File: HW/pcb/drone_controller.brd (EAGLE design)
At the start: 46.1 x 88.9 mm, 20 parts, among them J1 SM08B-SRSS-TB, U1 ICM-20600, U2 VXO7805-500, U3 CD40109BE

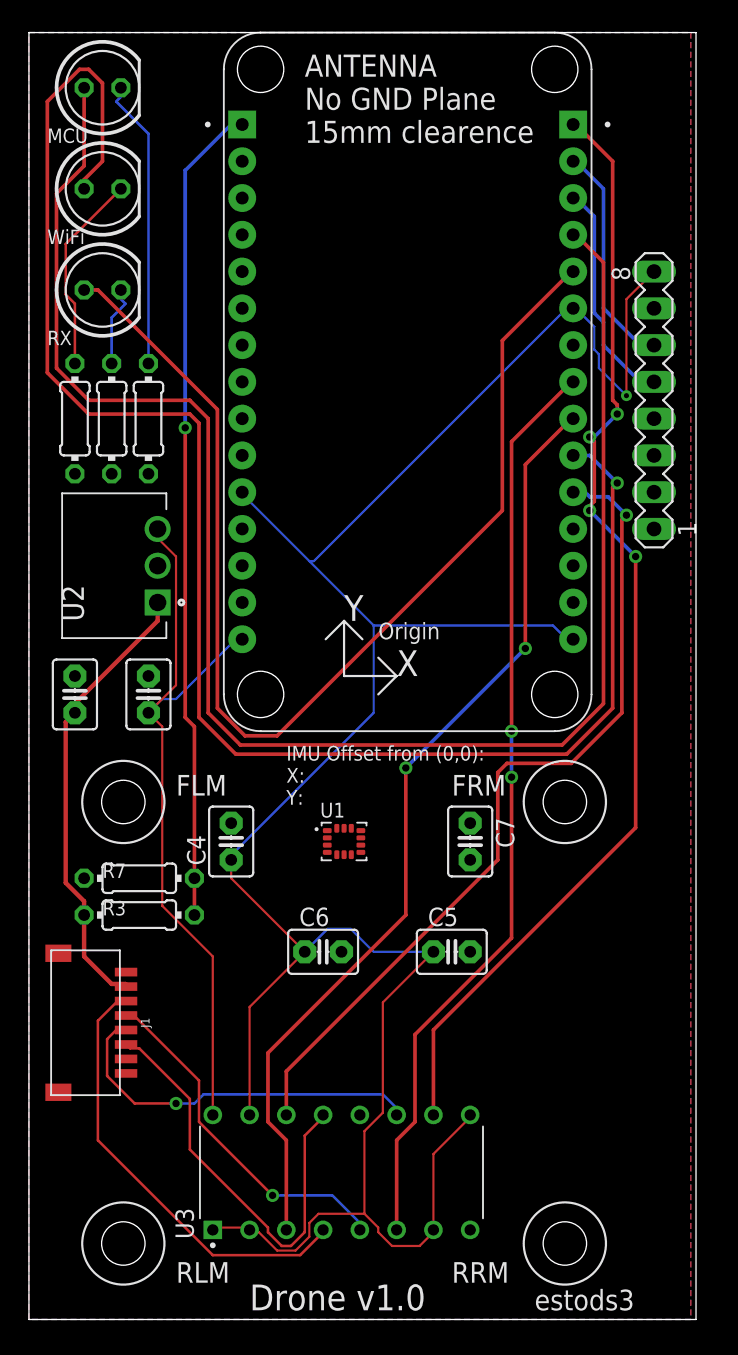
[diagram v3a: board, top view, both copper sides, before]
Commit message: removed 3.3V to 5V level shifter. not needed for this ESC (SpeedyBee 4-in-1 ESC). Placed components on board in more organized layout. Routed Board. All Airwires routed. Added Ground planes with stiching vias
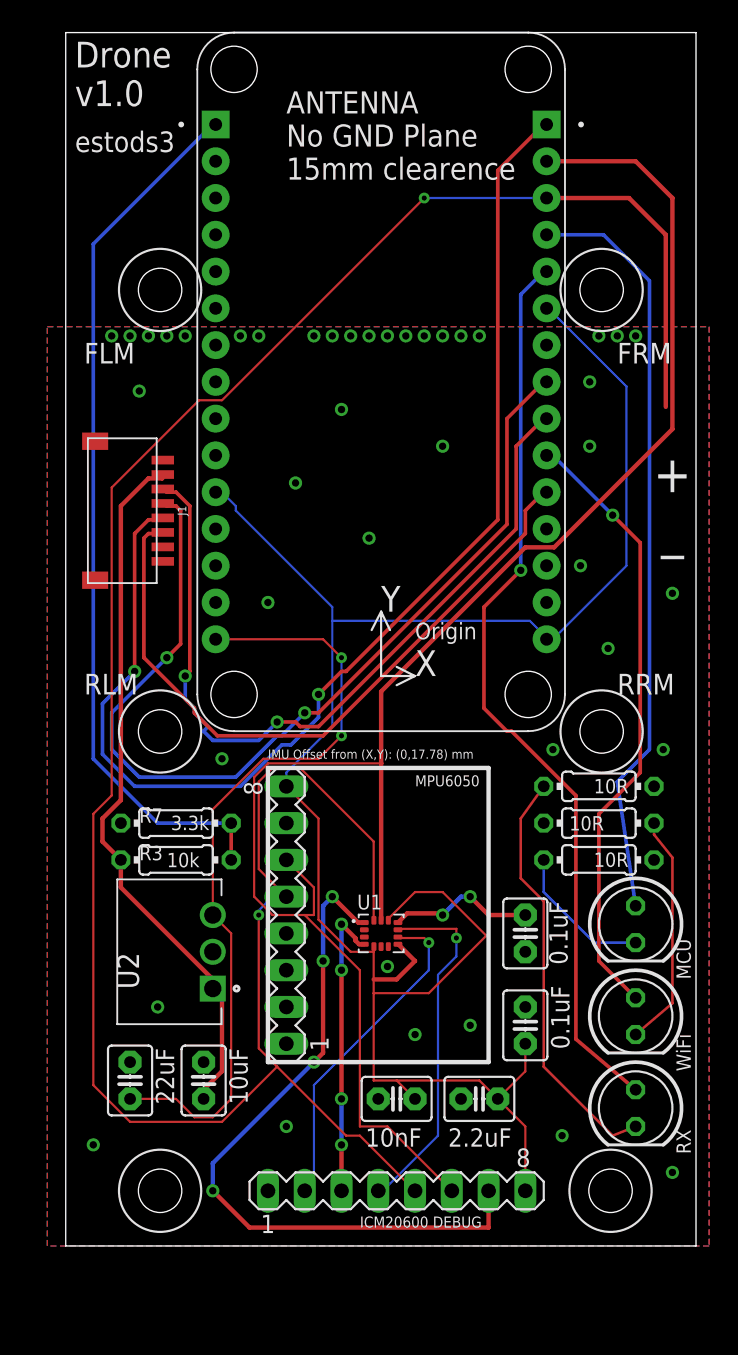
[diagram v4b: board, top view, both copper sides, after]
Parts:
- removed U3: CD40109BE, CD40109BE:DIP794W45P254L1969H508Q16
- added SV1: (no value), con-lstb:MA08-1
- moved LED4 68.5 mm to (40.6, 27.3), turned to 270 degrees
- moved LED5 68.0 mm to (40.6, 21.0), turned to 270 degrees
- moved LED6 67.5 mm to (40.6, 14.6), turned to 270 degrees
- moved R1 45.7 mm to (38.1, 34.3), turned to 180 degrees
- moved SV2 43.7 mm to (16.5, 27.9)
- moved R8 43.6 mm to (38.1, 31.8), turned to 0 degrees
- moved R2 42.2 mm to (38.1, 36.8), turned to 0 degrees
- moved J1 35.5 mm to (3.30, 55.9)
- moved C1 28.1 mm to (10.8, 16.5)
- moved U2 26.9 mm to (11.4, 22.9)
- moved C2 26.7 mm to (5.71, 16.5)
- moved C4 24.0 mm to (33.0, 20.3)
- moved C6 11.4 mm to (24.1, 15.2), turned to 180 degrees
- moved C5 10.3 mm to (29.8, 15.2), turned to 180 degrees
- moved C7 7.41 mm to (33.0, 26.7)
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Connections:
- removed net N$11: J1.6, U3.13
- removed net N$2: J1.3, U3.4
- removed net N$3: J1.4, U3.5
- removed net N$4: J1.5, U3.11
- net 3V3: now also SV1.8; no longer U3.1, U3.15, U3.2, U3.7, U3.9
- net 5V: no longer U3.16
- net AD0: now also SV1.7
- net FSYNC: now also SV1.4
- net GND: now also SV1.1; no longer U3.8
- net INT1: now also SV1.3
- net INT2: now also SV1.2
- net PWM_MOTOR_FL: now also J1.4; no longer U3.6
- net PWM_MOTOR_FR: now also J1.3; no longer U3.3
- net PWM_MOTOR_RL: now also J1.6; no longer U3.14
- net PWM_MOTOR_RR: now also J1.5; no longer U3.10
- net SCL: now also SV1.6
- net SDA: now also SV1.5
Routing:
- net SDA: track 15.7 -> 167.9 mm, vias 0 -> 2
- net SCL: track 15.7 -> 120.3 mm
- net GPIO_LED_WIFI_CONN: track 114.4 -> 42.6 mm
- net GPIO_LED_HEARTBEAT: track 115.2 -> 52.6 mm
- net AD0: track 0.00 -> 49.3 mm, vias 0 -> 4
- net 3V3: track 170.1 -> 138.7 mm, vias 1 -> 0
- net N$2: track 30.4 -> 0.00 mm
- net N$11: track 29.4 -> 0.00 mm
- net N$4: track 26.0 -> 0.00 mm, vias 1 -> 0
- net FSYNC: track 0.00 -> 24.6 mm, vias 0 -> 1
- net N$3: track 24.2 -> 0.00 mm, vias 1 -> 0
- net N$14: track 5.61 -> 29.0 mm
- net INT2: track 0.00 -> 23.0 mm, vias 0 -> 1
- net INT1: track 0.00 -> 20.7 mm, vias 0 -> 4
- net VCC: track 31.4 -> 49.3 mm
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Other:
- board size 46.1 x 88.9 mm -> 43.5 x 83.8 mm
- board text added: "+ _"
- board text added: "ICM20600 DEBUG"
- board text added: "IMU Offset from (X,Y): (0,17.78) mm"
- board text added: "MPU6050"
- board text removed: "IMU Offset from (0,0): X: Y:"
